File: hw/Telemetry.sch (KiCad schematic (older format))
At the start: 34 parts, among them J102 BOOT0, J103 SPORT, J104 SBUS, J105 USB_B_Micro, J106 UART_EXP, SW101 SW_Push, U101 STM32F303CBx, U102 IS25LP032D, X101 SG-310_SCF_8.000000MHZ

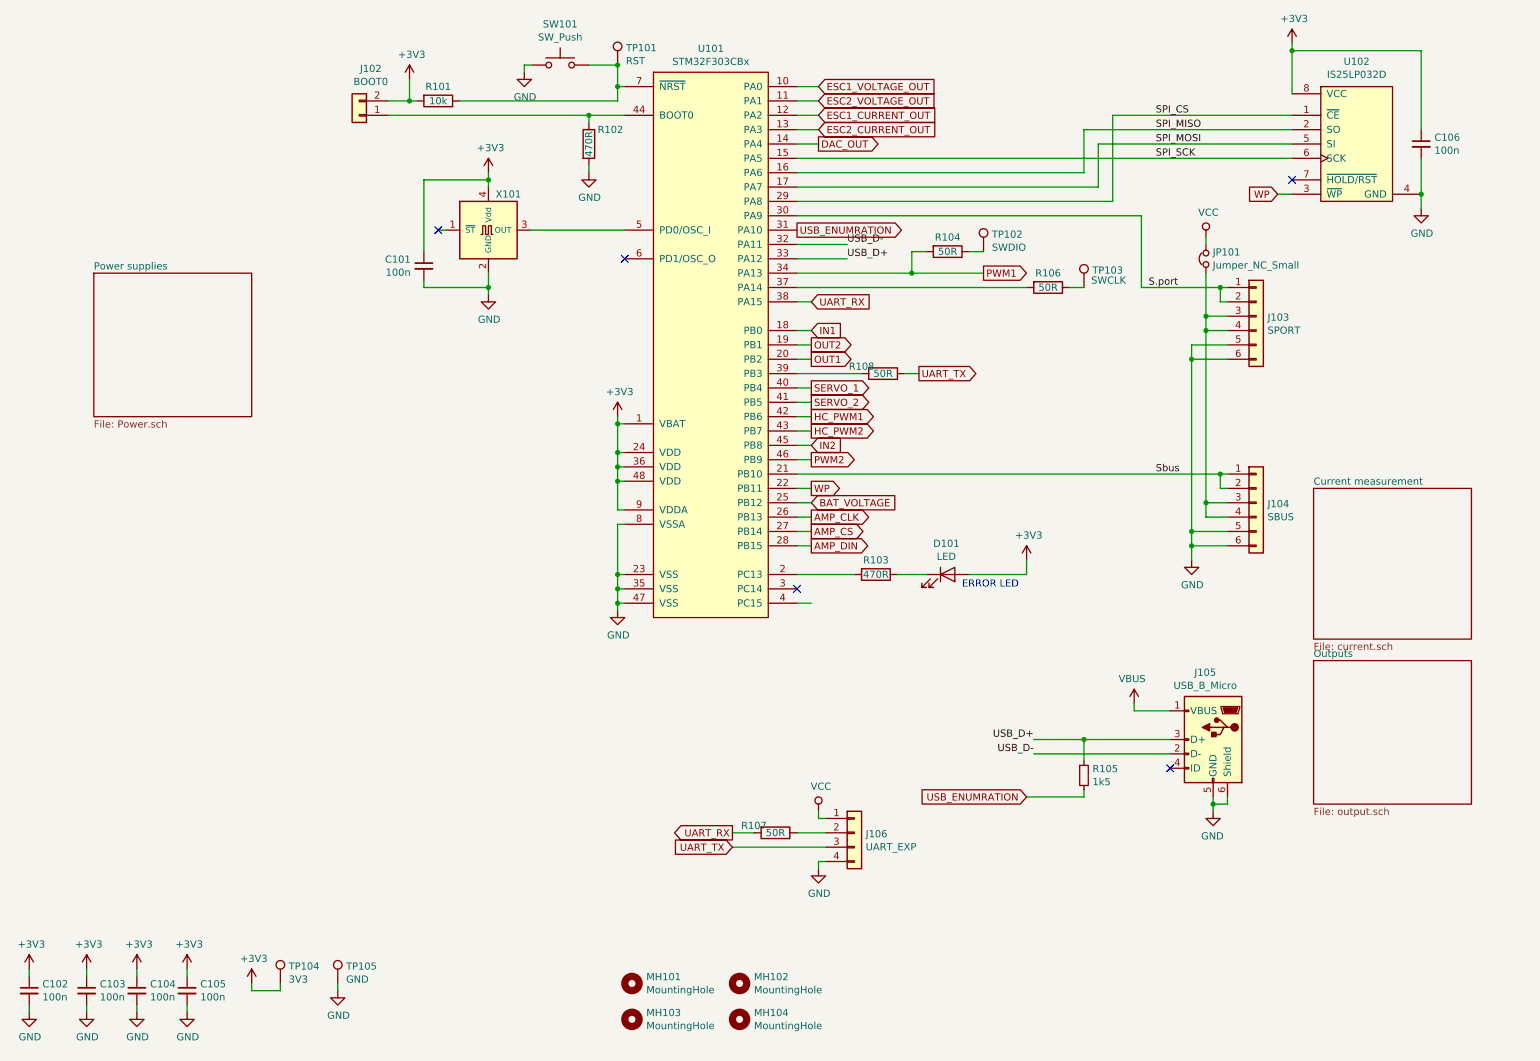
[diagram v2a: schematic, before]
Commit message: Changed High current pwm connectors to 5mm pitch versions
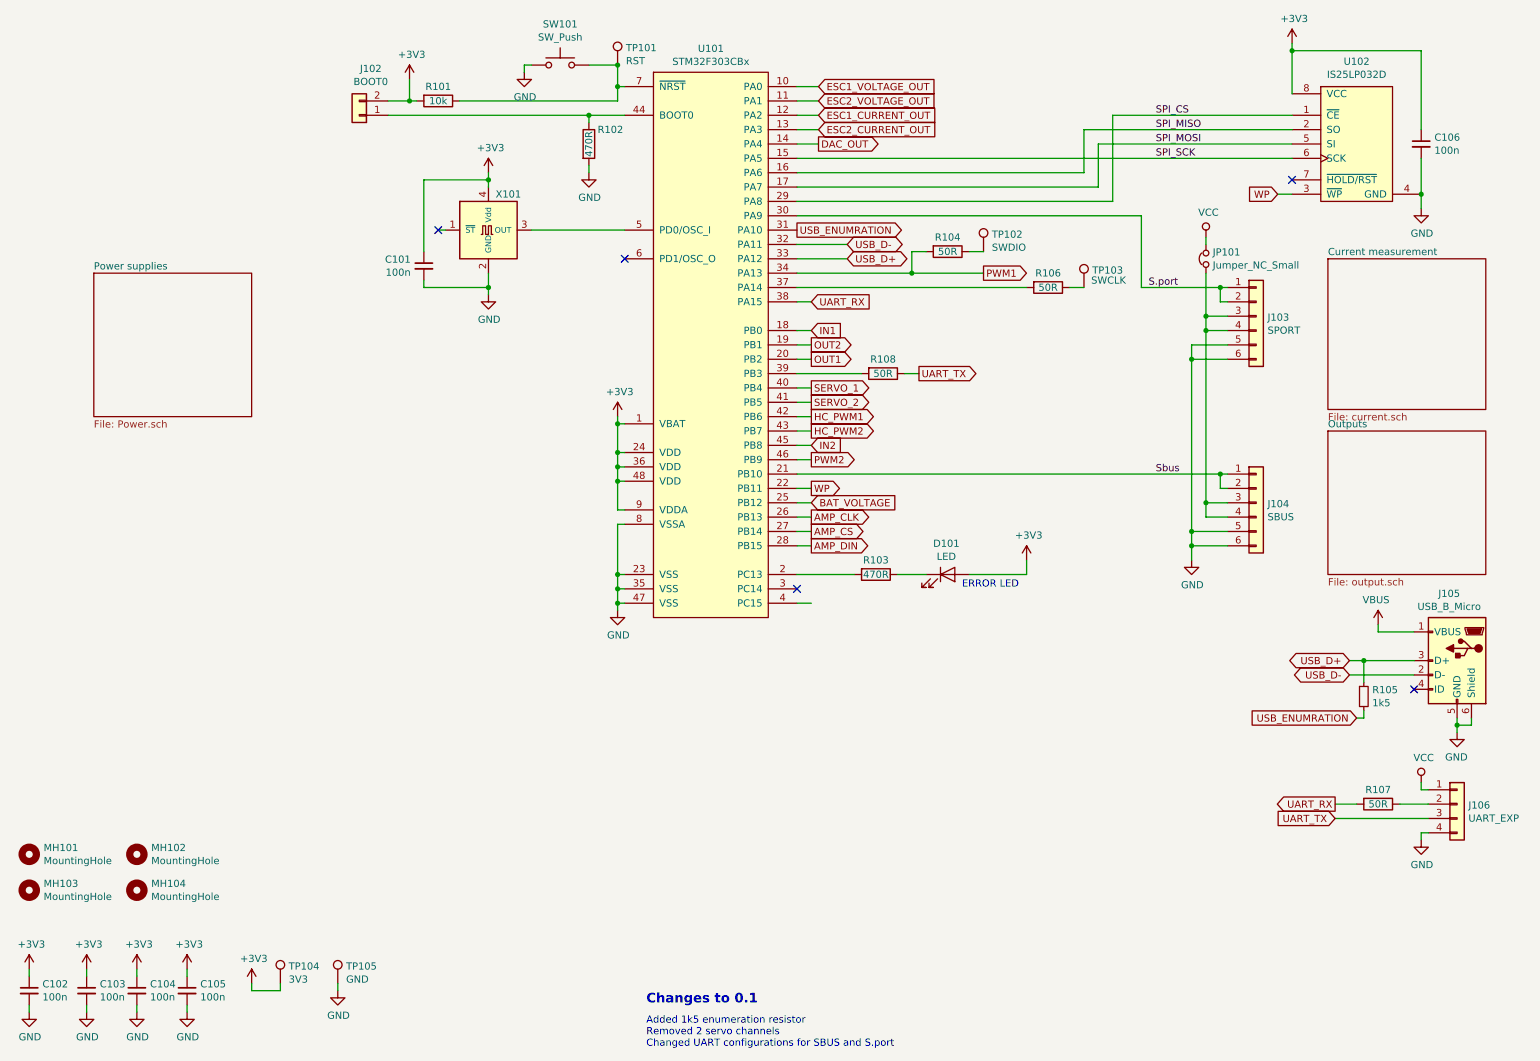
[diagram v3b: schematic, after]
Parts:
- JP101: footprint Pin_Headers:Pin_Header_Straight_1x02 -> Connector_PinHeader_2.54mm:PinHeader_1x02_P2.54mm_Vertical
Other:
- note added: "Added 1k5 enumeration resistor\nRemoved 2 servo channels\nChanged UART configurations for SBUS and S.port"
- note added: "Changes to 0.1\n"
- moved on the sheet: J105, J106, MH101, MH102, MH103, MH104, R105, R107

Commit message: BOM Generation for 1.1 version
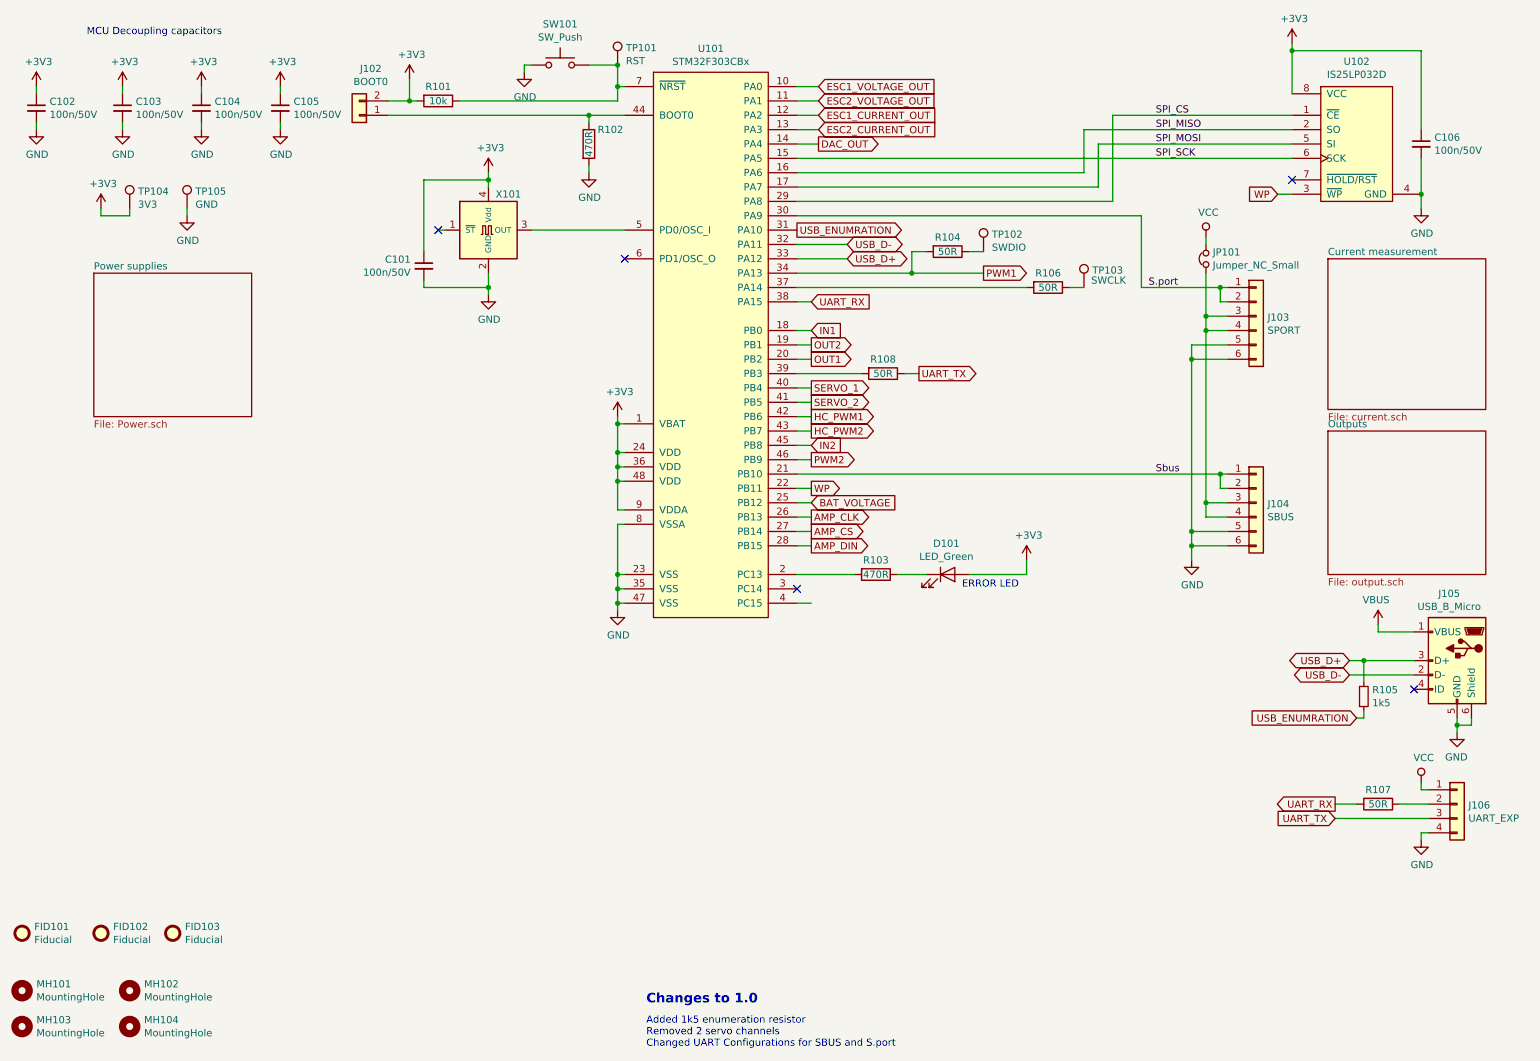
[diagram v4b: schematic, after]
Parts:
- added FID101, FID102, FID103: Fiducial, Fiducial:Fiducial_1mm_Mask2mm, symbol Mechanical:Fiducial
- C101, C102, C103, C104, C105, C106: value 100n -> 100n/50V
- D101: value LED -> LED_Green
- J102, J103, J104, J105, J106, JP101: Config (none) -> -prod
- SW101: Config (none) -> -prod; MPN (none) -> B3U-1000P; Manufacturer (none) -> Omron
- U101: MPN (none) -> STM32F303CB; Manufacturer (none) -> ST Microelectronics
- U102: MPN (none) -> IS25LP032D; Manufacturer (none) -> ISSI
- X101: Description (none) -> SMD Oscillator 8 MHz; MPN (none) -> SG-310_SCF_8.000000MHZ; Manufacturer (none) -> Epson
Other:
- note added: "Added 1k5 enumeration resistor\nRemoved 2 servo channels\nChanged UART Configurations for SBUS and S.port"
- note added: "Changes to 1.0\n"
- note added: "MCU Decoupling capacitors"
- note removed: "Added 1k5 enumeration resistor\nRemoved 2 servo channels\nChanged UART configurations for SBUS and S.port"
- note removed: "Changes to 0.1\n"
- moved on the sheet: C102, C103, C104, C105, MH101, MH102, MH103, MH104, TP104, TP105

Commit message: DAC Amplifier improvements
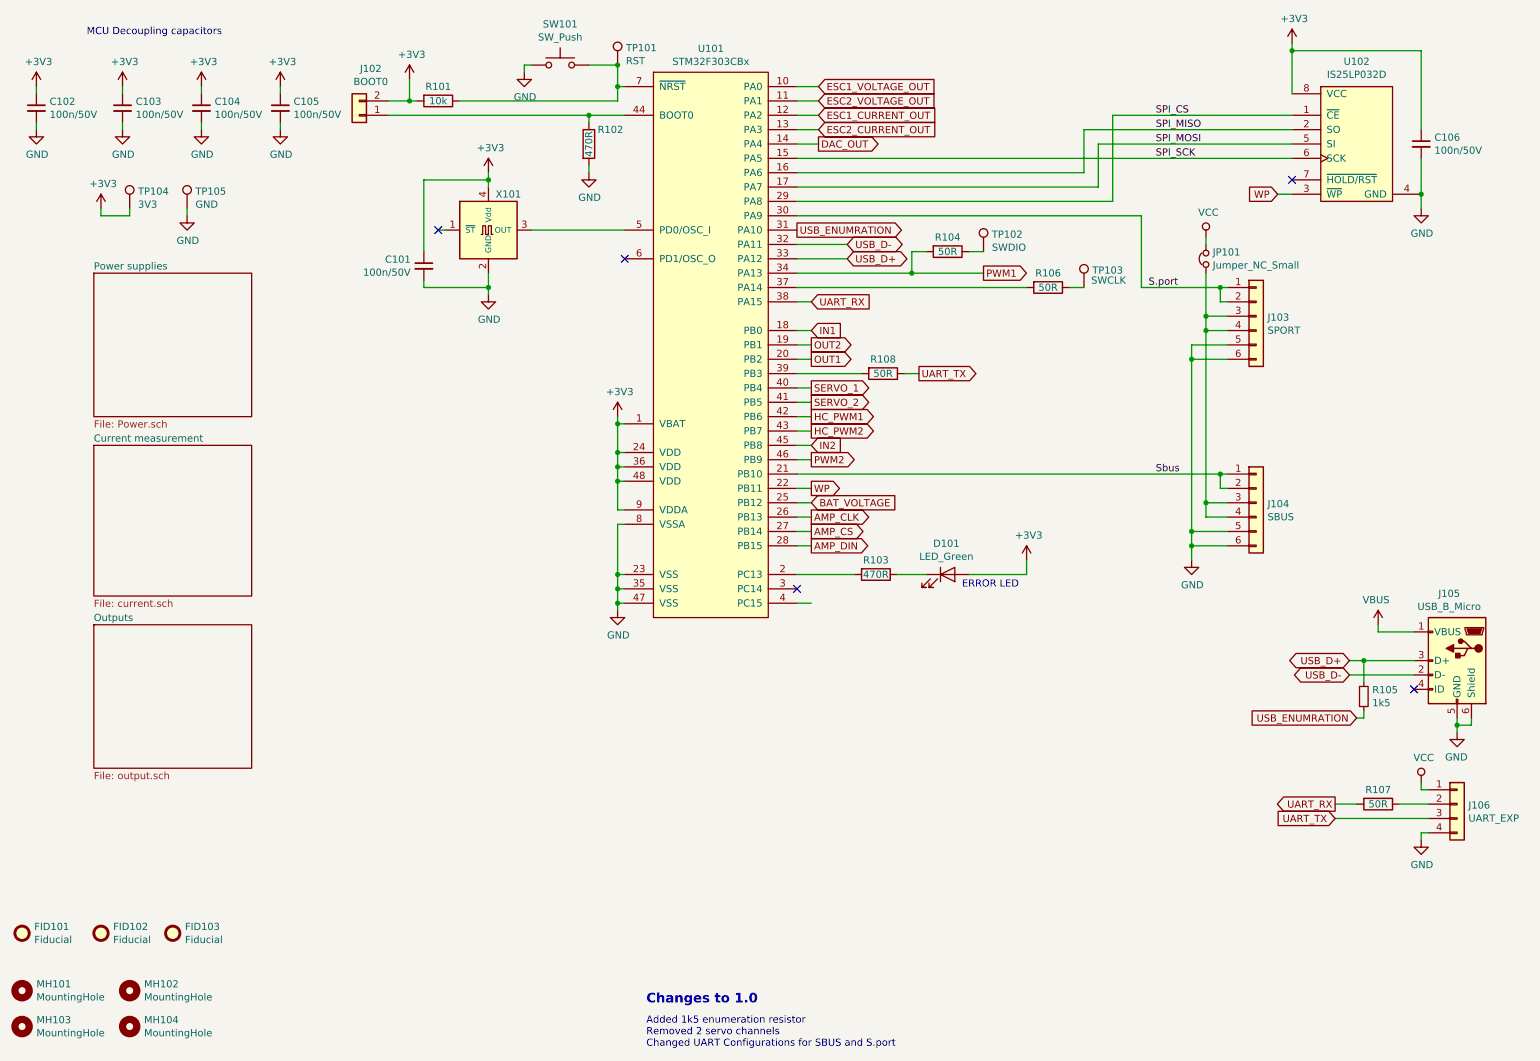
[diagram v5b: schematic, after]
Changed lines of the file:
@@
 $EndSheet
 $Sheet
-S 9750 2200 1100 1050
+S 1150 3500 1100 1050
 U 5CE3A6F3
 F0 "Current measurement" 50
@@
 Connection ~ 4800 1000
 $Sheet
-S 9750 3400 1100 1000
+S 1150 4750 1100 1000
 U 5CEA3FFC
 F0 "Outputs" 50

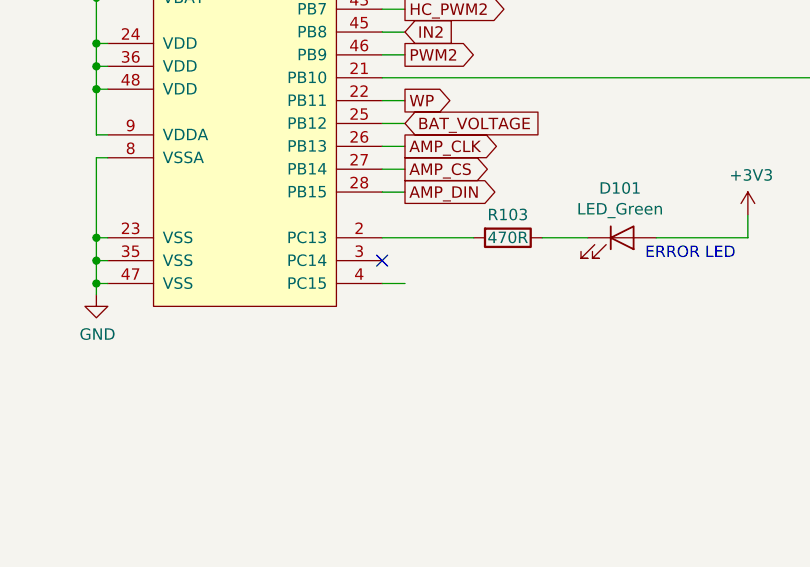
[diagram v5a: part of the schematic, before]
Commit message: Added additional opamp to DAC output as a buffer.
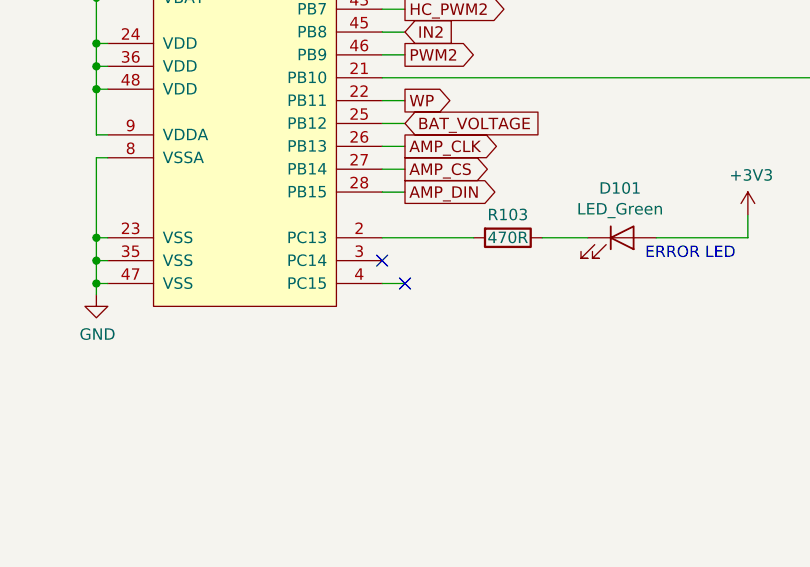
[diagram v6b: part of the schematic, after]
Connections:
- no-connect marks 5 -> 6
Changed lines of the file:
@@
 Sheet 1 4
 Title "RC Telemetry board"
-Date "2020-02-23"
+Date "2020-02-24"
 Rev "1.1"
 Comp "www.findersee.fi"
@@
 	1    0    0    -1
 $EndComp
+NoConn ~ 6150 4600
 $EndSCHEMATC

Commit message: Routing update
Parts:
- added JP102, JP103: Jumper_NC_Small, Resistor_SMD:R_0402_1005Metric, symbol Device:Jumper_NC_Small
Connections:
- net +3V3: now also JP103.2
- net VCC: now also JP102.2; no longer J106.1 (Pin_1)
- new net: J106.1 (Pin_1), JP102.1, JP103.1
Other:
- moved on the sheet: J106, R107
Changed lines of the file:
@@
 L power:GND #PWR0122
 U 1 1 5CE5F3AC
-P 10400 6250
-F 0 "#PWR0122" H 10400 6000 50  0001 C CNN
-F 1 "GND" H 10405 6077 50  0000 C CNN
-F 2 "" H 10400 6250 50  0001 C CNN
-F 3 "" H 10400 6250 50  0001 C CNN
-	1    10400 6250
-	1    0    0    -1
-$EndComp
-Wire Wire Line
-	10450 6200 10400 6200
-Wire Wire Line
-	10400 6200 10400 6250
-$Comp
-L Connector_Generic:Conn_01x04 J106
-U 1 1 5CE6386B
-P 10650 6000
-F 0 "J106" H 10729 5992 50  0000 L CNN
-F 1 "UART_EXP" H 10729 5901 50  0000 L CNN
-F 2 "Connector_PinHeader_2.54mm:PinHeader_2x02_P2.54mm_Vertical" H 10650 6000 50  0001 C CNN
-F 3 "~" H 10650 6000 50  0001 C CNN
-F 4 "-prod" H 10650 6000 50  0001 C CNN "Config"
-	1    10650 6000
-	1    0    0    -1
-$EndComp
-Wire Wire Line
-	10450 5900 10400 5900
-Wire Wire Line
-	10400 5900 10400 5850
-$Comp
-L power:VCC #PWR0123
-U 1 1 5CE67EB7
-P 10400 5850
-F 0 "#PWR0123" H 10400 5700 50  0001 C CNN
-F 1 "VCC" H 10417 6023 50  0000 C CNN
-F 2 "" H 10400 5850 50  0001 C CNN
-F 3 "" H 10400 5850 50  0001 C CNN
-	1    10400 5850
-	1    0    0    -1
-$EndComp
+P 6450 6400
+F 0 "#PWR0122" H 6450 6150 50  0001 C CNN
+F 1 "GND" H 6455 6227 50  0000 C CNN
+F 2 "" H 6450 6400 50  0001 C CNN
+F 3 "" H 6450 6400 50  0001 C CNN
+	1    6450 6400
+	1    0    0    -1
+$EndComp
+Wire Wire Line
+	6500 6350 6450 6350
+Wire Wire Line
+	6450 6350 6450 6400
 Text GLabel 6150 3900 2    50   Input ~ 0
 BAT_VOLTAGE
@@
 	1    0    0    -1
 $EndComp
-Text GLabel 9800 6000 0    50   Output ~ 0
+Text GLabel 5850 6150 0    50   Output ~ 0
 UART_RX
-Text GLabel 9800 6100 0    50   Input ~ 0
+Text GLabel 5850 6250 0    50   Input ~ 0
 UART_TX
 Text GLabel 6150 3100 2    50   Output ~ 0
@@
 L Device:R R107
 U 1 1 5E51659E
-P 10100 6000
-F 0 "R107" V 10000 6000 50  0000 C CNN
-F 1 "50R" V 10100 6000 50  0000 C CNN
-F 2 "Resistor_SMD:R_0603_1608Metric_Pad1.05x0.95mm_HandSolder" V 10030 6000 50  0001 C CNN
-F 3 "~" H 10100 6000 50  0001 C CNN
-	1    10100 6000
+P 6150 6150
+F 0 "R107" V 6050 6150 50  0000 C CNN
+F 1 "50R" V 6150 6150 50  0000 C CNN
+F 2 "Resistor_SMD:R_0603_1608Metric_Pad1.05x0.95mm_HandSolder" V 6080 6150 50  0001 C CNN
+F 3 "~" H 6150 6150 50  0001 C CNN
+	1    6150 6150
 	0    1    1    0
 $EndComp
 Wire Wire Line
-	9950 6000 9800 6000
-Wire Wire Line
-	10250 6000 10450 6000
+	6000 6150 5850 6150
+Wire Wire Line
+	6300 6150 6500 6150
 $Comp
 L Device:R R108
@@
 	6050 3000 6500 3000
 Wire Wire Line
-	9800 6100 10450 6100
+	5850 6250 6500 6250
 Wire Wire Line
 	4800 4050 4800 4400
@@
 $EndComp
 NoConn ~ 6150 4600
+$Comp
+L power:VCC #PWR0123
+U 1 1 5CE67EB7
+P 6100 5350
+F 0 "#PWR0123" H 6100 5200 50  0001 C CNN
+F 1 "VCC" H 6117 5523 50  0000 C CNN
+F 2 "" H 6100 5350 50  0001 C CNN
+F 3 "" H 6100 5350 50  0001 C CNN
+	1    6100 5350
+	1    0    0    -1
+$EndComp
+$Comp
+L power:+3V3 #PWR0144
+U 1 1 5E59175F
+P 6500 5350
+F 0 "#PWR0144" H 6500 5200 50  0001 C CNN
+F 1 "+3V3" H 6515 5523 50  0000 C CNN
+F 2 "" H 6500 5350 50  0001 C CNN
+F 3 "" H 6500 5350 50  0001 C CNN
+	1    6500 5350
+	1    0    0    -1
+$EndComp
+Wire Wire Line
+	6100 5750 6100 5650
+Wire Wire Line
+	6100 5750 6500 5750
+Wire Wire Line
+	6100 5450 6100 5350
+Wire Wire Line
+	6500 5350 6500 5450
+Wire Wire Line
+	6500 5650 6500 5750
+$Comp
+L Connector_Generic:Conn_01x04 J106
+U 1 1 5CE6386B
+P 6700 6150
+F 0 "J106" H 6779 6142 50  0000 L CNN
+F 1 "UART_EXP" H 6779 6051 50  0000 L CNN
+F 2 "Connector_PinHeader_2.54mm:PinHeader_2x02_P2.54mm_Vertical" H 6700 6150 50  0001 C CNN
+F 3 "~" H 6700 6150 50  0001 C CNN
+F 4 "-prod" H 6700 6150 50  0001 C CNN "Config"
+	1    6700 6150
+	1    0    0    -1
+$EndComp
+Connection ~ 6500 5750
+$Comp
+L Device:Jumper_NC_Small JP103
+U 1 1 5E5F175F
+P 6500 5550
+F 0 "JP103" V 6550 5850 50  0000 R CNN
+F 1 "Jumper_NC_Small" V 6455 5503 50  0001 R CNN
+F 2 "Resistor_SMD:R_0402_1005Metric" H 6500 5550 50  0001 C CNN
+F 3 "~" H 6500 5550 50  0001 C CNN
+F 4 "dnp" H 6500 5550 50  0001 C CNN "Config"
+	1    6500 5550
+	0    -1   -1   0
+$EndComp
+$Comp
+L Device:Jumper_NC_Small JP102
+U 1 1 5E5F3931
+P 6100 5550
+F 0 "JP102" V 6150 5850 50  0000 R CNN
+F 1 "Jumper_NC_Small" V 6050 6300 50  0001 R CNN
+F 2 "Resistor_SMD:R_0402_1005Metric" H 6100 5550 50  0001 C CNN
+F 3 "~" H 6100 5550 50  0001 C CNN
+F 4 "dnp" H 6100 5550 50  0001 C CNN "Config"
+	1    6100 5550
+	0    -1   -1   0
+$EndComp
+Wire Wire Line
+	6500 5750 6500 6050
 $EndSCHEMATC
